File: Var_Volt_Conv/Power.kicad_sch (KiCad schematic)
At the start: 67 parts

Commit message: Annotated schematic symbols
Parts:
- gave numbers to parts that had none: 67

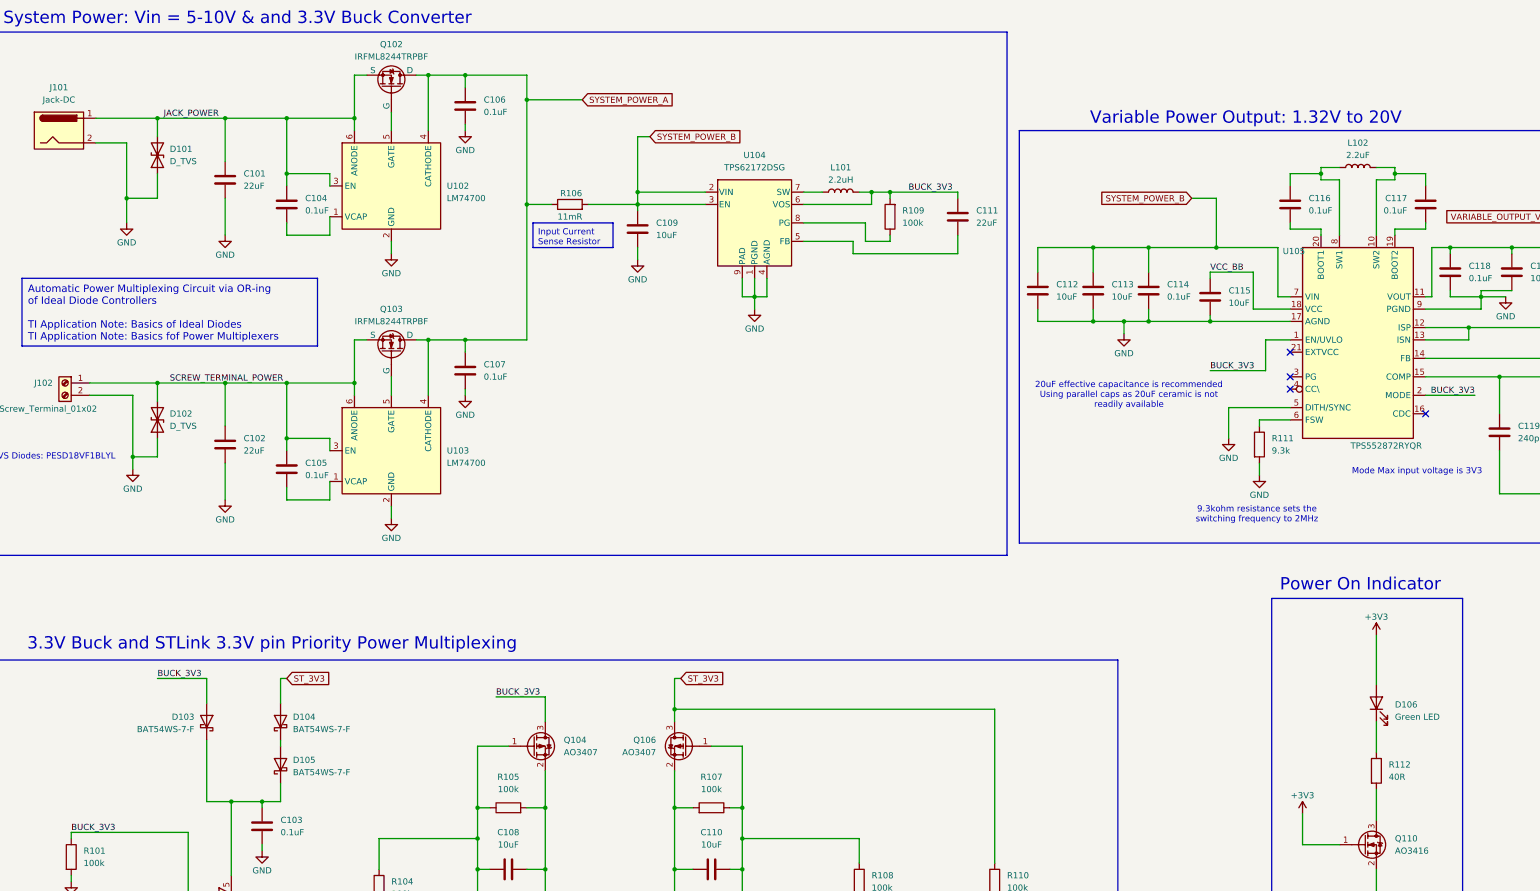
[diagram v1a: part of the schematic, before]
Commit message: Fixed ERC issues
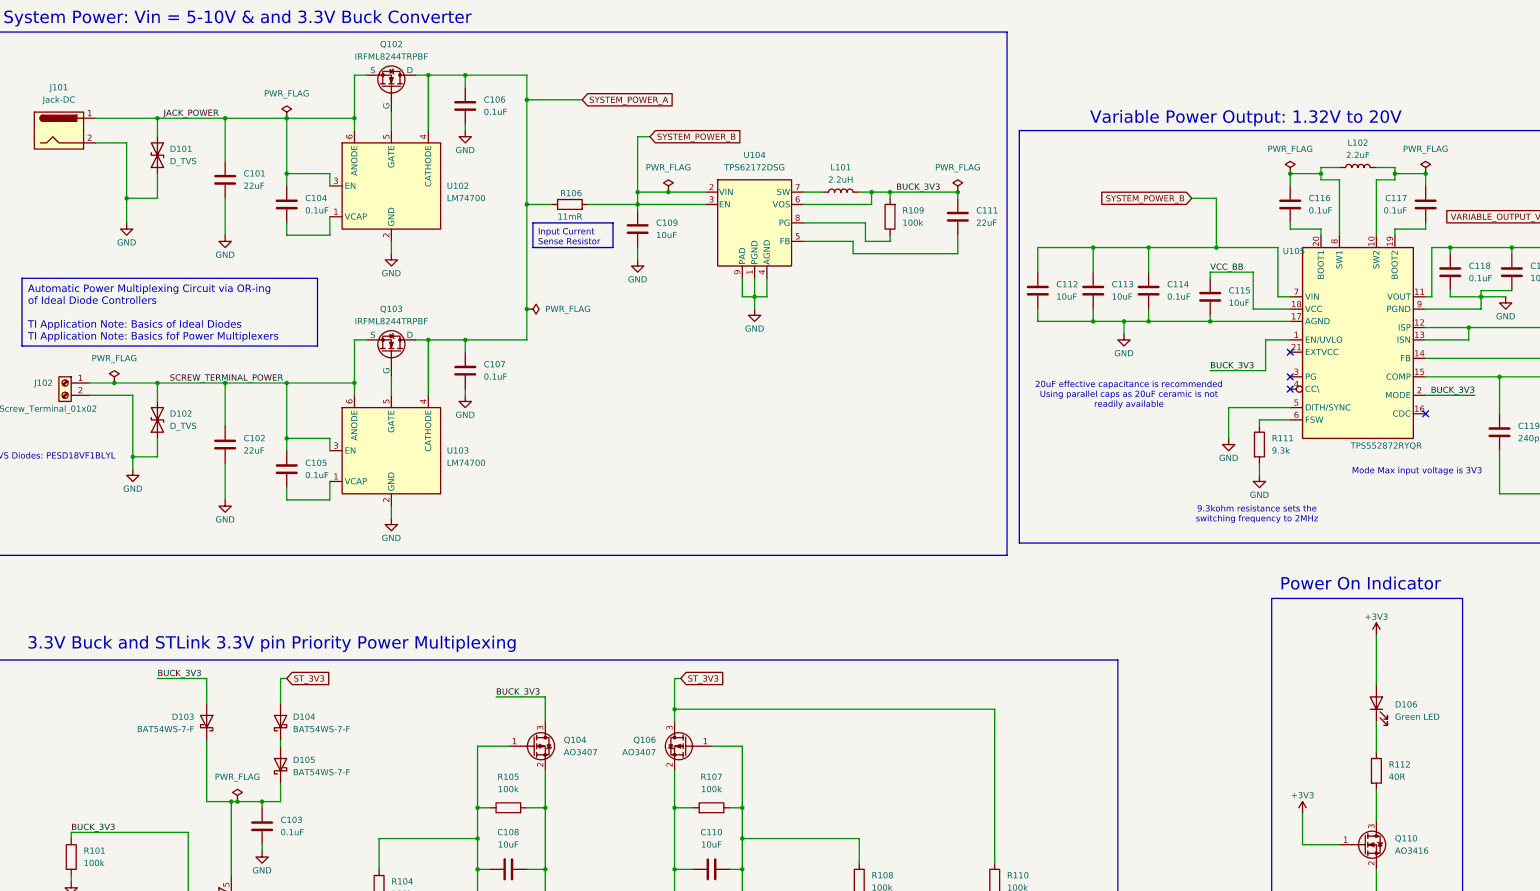
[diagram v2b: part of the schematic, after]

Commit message: Add footprints and correct LCD pin numbering
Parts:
- D102: footprint (none) -> Diode_SMD:D_SOD-882
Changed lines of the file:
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@@
 			)
 		)
-		(property "Footprint" ""
+		(property "Footprint" "Diode_SMD:D_SOD-882"
 			(at 52.07 135.89 0)
 			(effects

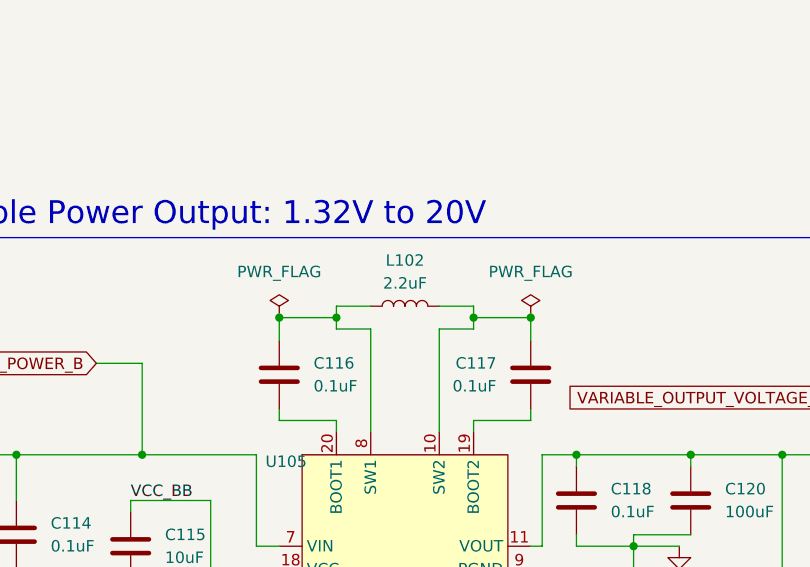
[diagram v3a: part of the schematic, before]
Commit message: Add footprints for all capacitors, and record cap part names
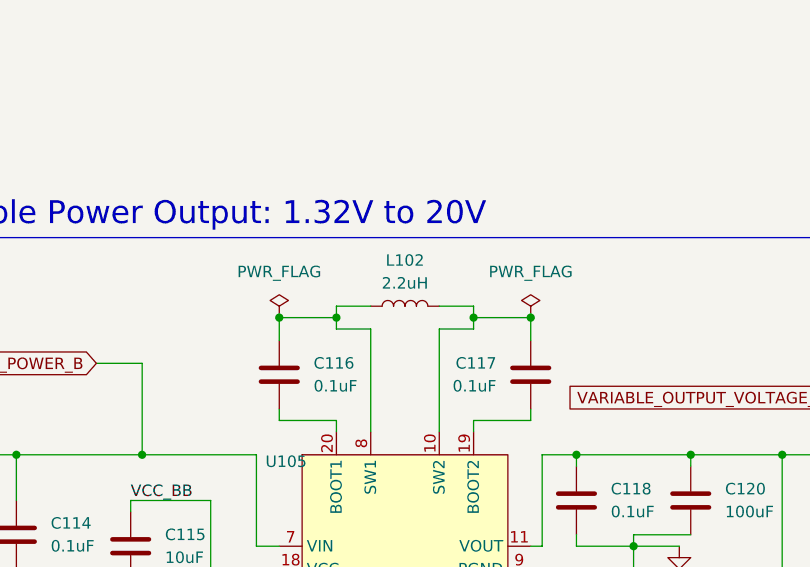
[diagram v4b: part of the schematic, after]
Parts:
- C101, C102, C111: footprint (none) -> Capacitor_SMD:C_1206_3216Metric
- C103, C104, C105, C106, C107, C114, C116, C117, C118, C121: footprint (none) -> Capacitor_SMD:C_0402_1005Metric
- C108, C109, C110, C112, C113, C115: footprint (none) -> Capacitor_SMD:C_0805_2012Metric
- C119, C122, C123: footprint (none) -> Capacitor_SMD:C_0603_1608Metric
- C120: footprint (none) -> Capacitor_SMD:CP_Elec_6.3x7.7
- L102: value 2.2uF -> 2.2uH
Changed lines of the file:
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@@
 			)
 		)
-		(property "Footprint" ""
+		(property "Footprint" "Capacitor_SMD:C_0402_1005Metric"
 			(at 79.7052 95.25 0)
 			(effects
@@
 			)
 		)
-		(property "Footprint" ""
+		(property "Footprint" "Capacitor_SMD:C_1206_3216Metric"
 			(at 67.0052 144.78 0)
 			(effects
@@
 			)
 		)
-		(property "Footprint" ""
+		(property "Footprint" "Capacitor_SMD:C_0402_1005Metric"
 			(at 257.5052 113.03 0)
 			(effects
@@
 			)
 		)
-		(property "Footprint" ""
+		(property "Footprint" "Capacitor_SMD:C_0402_1005Metric"
 			(at 74.6252 223.52 0)
 			(effects
@@
 			)
 		)
-		(property "Footprint" ""
+		(property "Footprint" "Capacitor_SMD:CP_Elec_6.3x7.7"
 			(at 332.4352 109.22 0)
 			(effects
@@
 			)
 		)
-		(property "Footprint" ""
+		(property "Footprint" "Capacitor_SMD:C_0402_1005Metric"
 			(at 345.1352 149.86 0)
 			(effects
@@
 			)
 		)
-		(property "Footprint" ""
+		(property "Footprint" "Capacitor_SMD:C_1206_3216Metric"
 			(at 218.1352 97.79 0)
 			(effects
@@
 			)
 		)
-		(property "Footprint" ""
+		(property "Footprint" "Capacitor_SMD:C_0805_2012Metric"
 			(at 128.27 227.6348 0)
 			(effects
@@
 			)
 		)
-		(property "Footprint" ""
+		(property "Footprint" "Capacitor_SMD:C_0805_2012Metric"
 			(at 234.6452 113.03 0)
 			(effects
@@
 			)
 		)
-		(property "Footprint" ""
+		(property "Footprint" "Capacitor_SMD:C_0603_1608Metric"
 			(at 354.0252 201.93 0)
 			(effects
@@
 			)
 		)
-		(property "Footprint" ""
+		(property "Footprint" "Capacitor_SMD:C_0603_1608Metric"
 			(at 388.3152 201.93 0)
 			(effects
@@
 			)
 		)
-		(property "Footprint" ""
+		(property "Footprint" "Capacitor_SMD:C_0402_1005Metric"
 			(at 79.7052 149.86 0)
 			(effects
@@
 			)
 		)
-		(property "Footprint" ""
+		(property "Footprint" "Capacitor_SMD:C_0805_2012Metric"
 			(at 246.0752 113.03 0)
 			(effects
@@
 			)
 		)
-		(property "Value" "2.2uF"
+		(property "Value" "2.2uH"
 			(at 299.72 81.28 90)
 			(effects
@@
 			)
 		)
-		(property "Footprint" ""
+		(property "Footprint" "Capacitor_SMD:C_0603_1608Metric"
 			(at 329.8952 142.24 0)
 			(effects
@@
 			)
 		)
-		(property "Footprint" ""
+		(property "Footprint" "Capacitor_SMD:C_0402_1005Metric"
 			(at 116.5352 129.54 0)
 			(effects
@@
 			)
 		)
-		(property "Footprint" ""
+		(property "Footprint" "Capacitor_SMD:C_0402_1005Metric"
 			(at 312.7248 95.25 0)
 			(effects
@@
 			)
 		)
-		(property "Footprint" ""
+		(property "Footprint" "Capacitor_SMD:C_0805_2012Metric"
 			(at 270.2052 114.3 0)
 			(effects
@@
 			)
 		)
-		(property "Footprint" ""
+		(property "Footprint" "Capacitor_SMD:C_0402_1005Metric"
 			(at 286.7152 95.25 0)
 			(effects
@@
 			)
 		)
-		(property "Footprint" ""
+		(property "Footprint" "Capacitor_SMD:C_0402_1005Metric"
 			(at 116.5352 74.93 0)
 			(effects
@@
 			)
 		)
-		(property "Footprint" ""
+		(property "Footprint" "Capacitor_SMD:C_1206_3216Metric"
 			(at 67.0052 90.17 0)
 			(effects
@@
 			)
 		)
-		(property "Footprint" ""
+		(property "Footprint" "Capacitor_SMD:C_0805_2012Metric"
 			(at 152.0952 100.33 0)
 			(effects
@@
 			)
 		)
-		(property "Footprint" ""
+		(property "Footprint" "Capacitor_SMD:C_0402_1005Metric"
 			(at 319.7352 109.22 0)
 			(effects
@@
 			)
 		)
-		(property "Footprint" ""
+		(property "Footprint" "Capacitor_SMD:C_0805_2012Metric"
 			(at 162.56 227.6348 0)
 			(effects

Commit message: Add inductor footprint
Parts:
- L101, L102: footprint (none) -> Inductor_SMD:L_Sunlord_MWSA0503S
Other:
- note added: "System Power: Vin = 3-17V & and 3.3V Buck Converter"
- note removed: "System Power: Vin = 5-10V & and 3.3V Buck Converter"
- moved on the sheet: C101, C102, C103, C104, C105, C106, C107, C108, C109, C110, C111, C112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

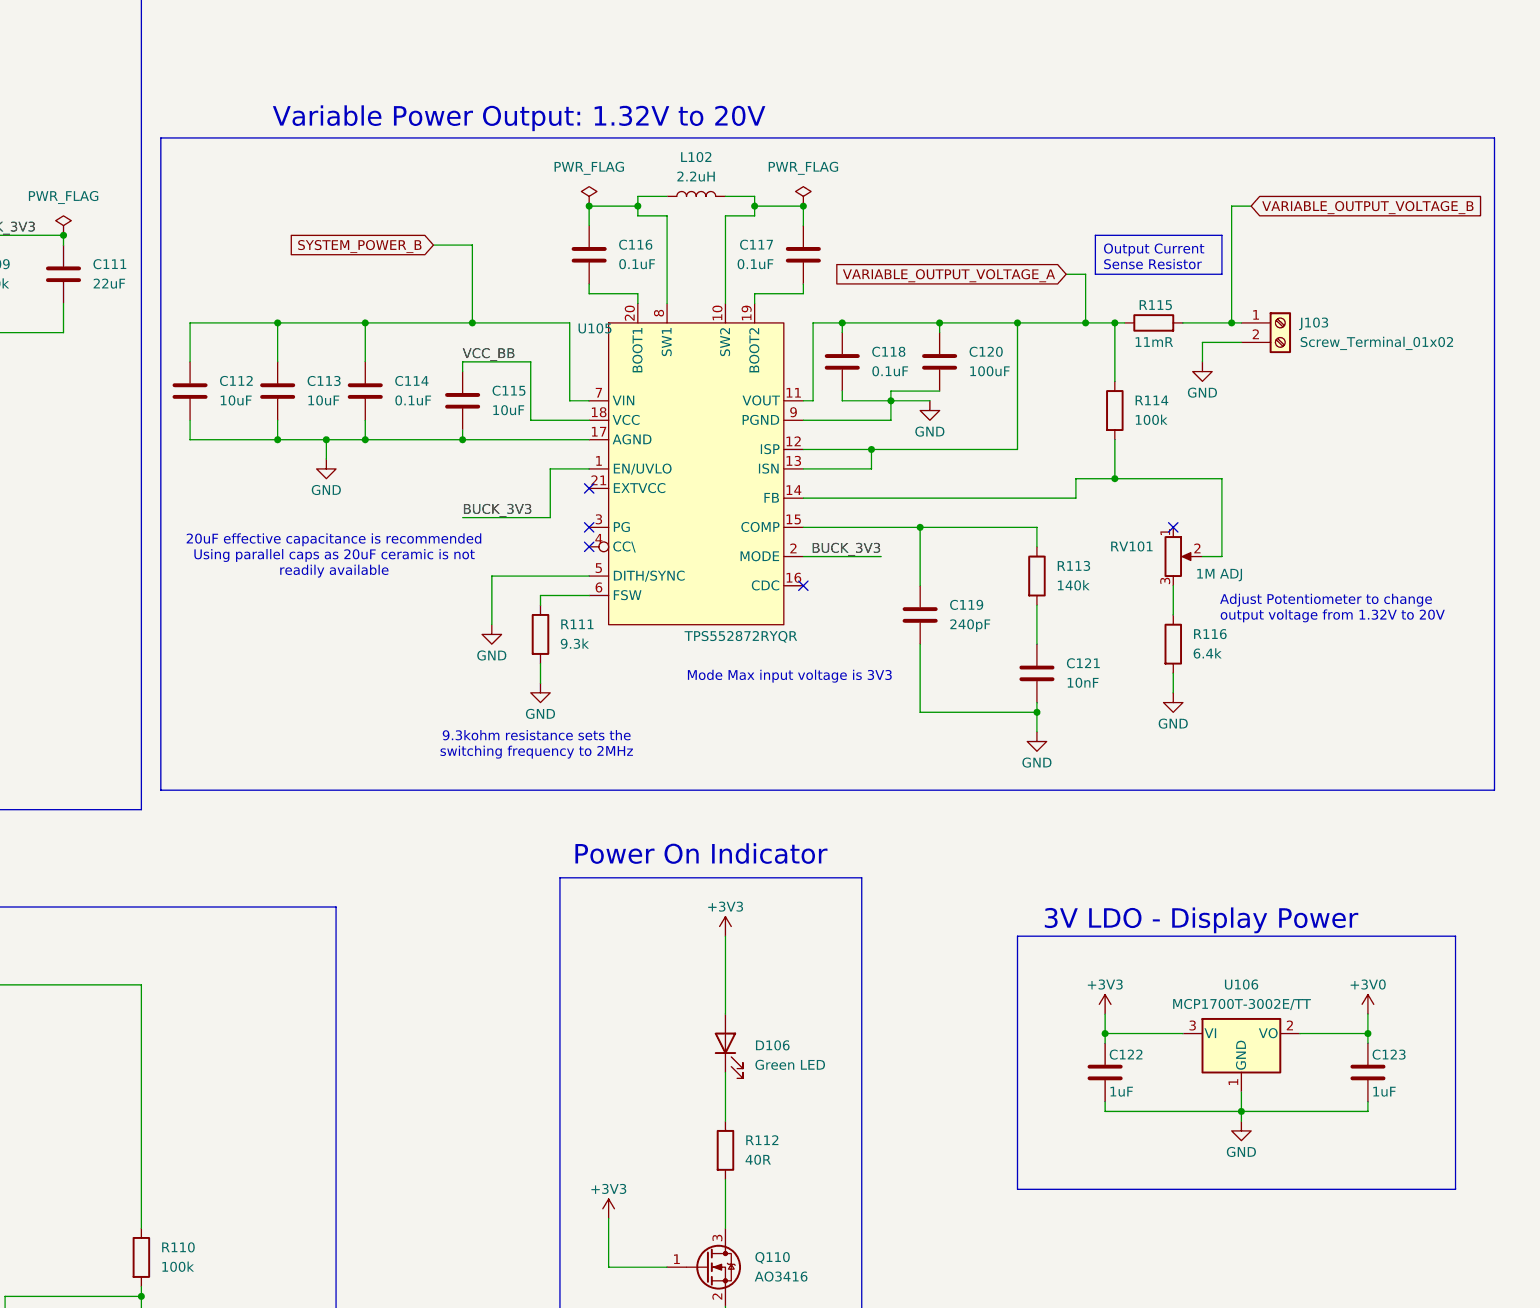
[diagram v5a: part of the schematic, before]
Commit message: Added footprints to all components except the connectors and buck-boost converter
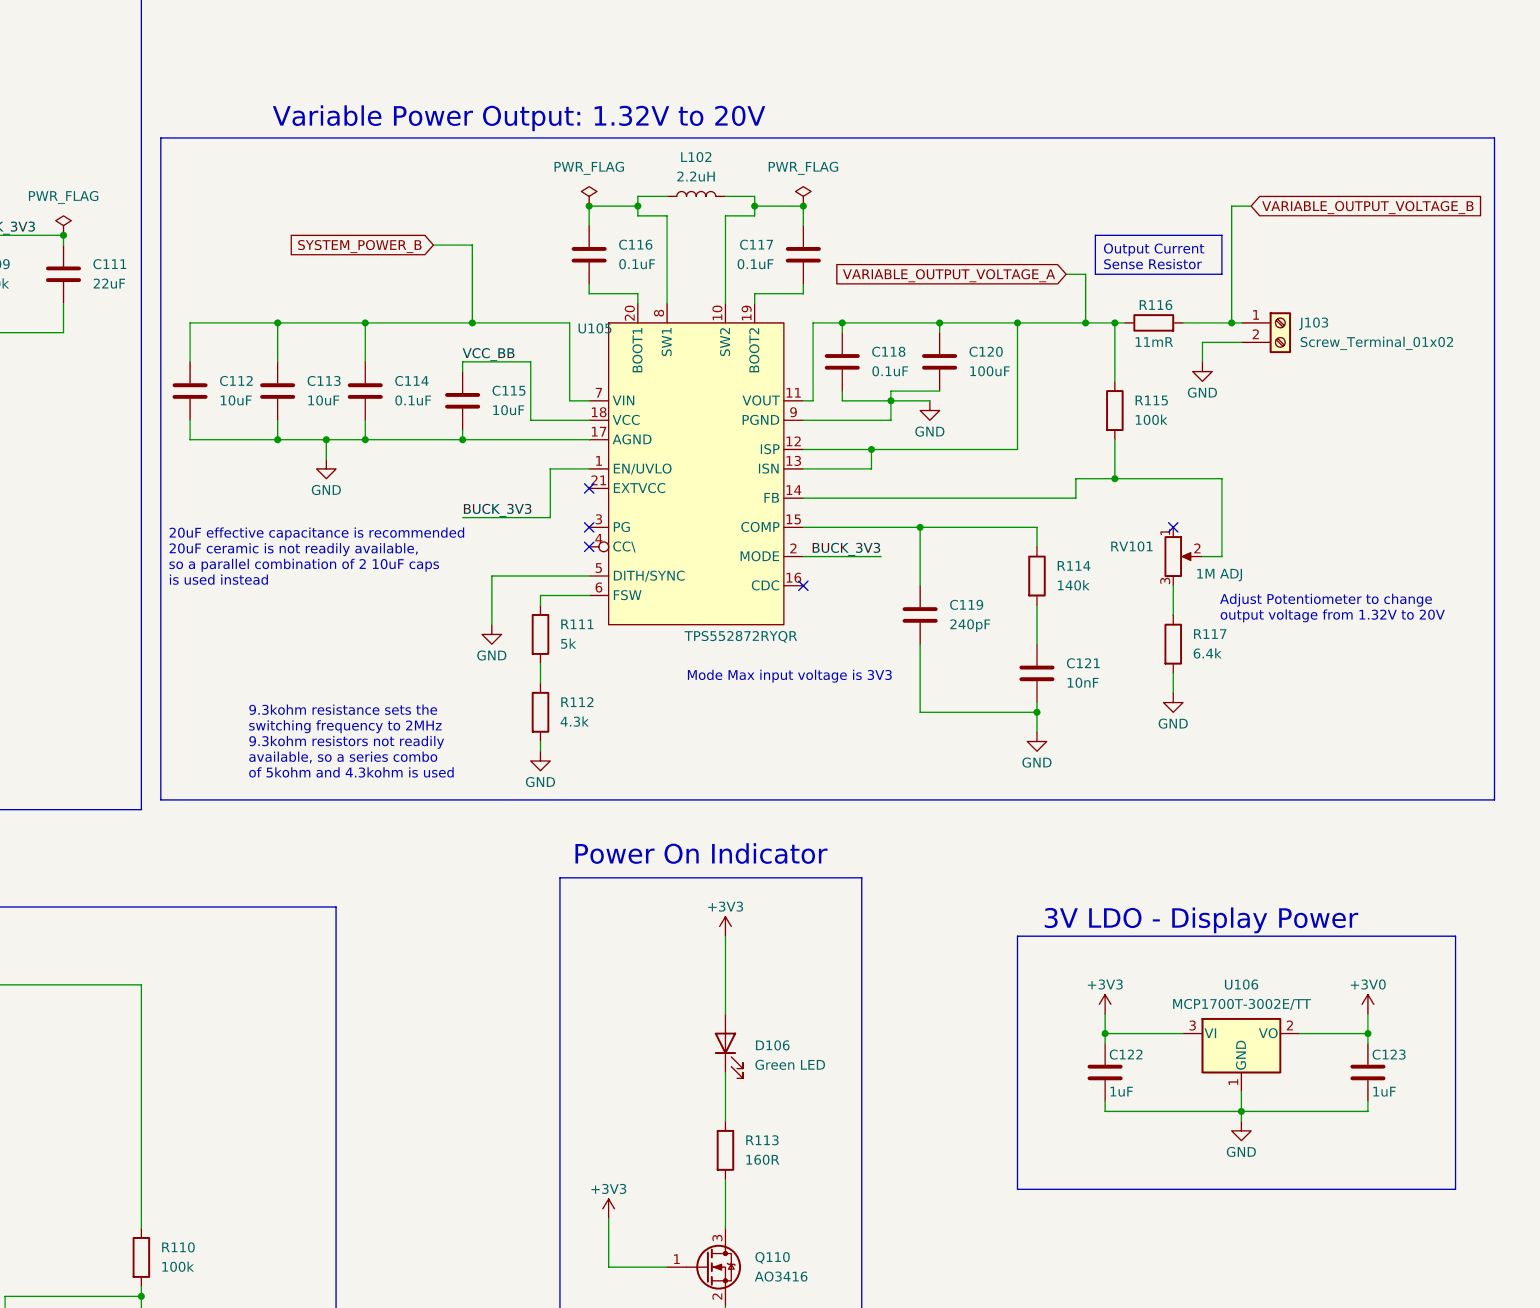
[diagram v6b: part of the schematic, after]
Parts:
- added R112: 4.3k, Resistor_SMD:R_0805_2012Metric, symbol Device:R
- R101, R102, R103, R104, R105, R107, R108, R109, R110: footprint (none) -> Resistor_SMD:R_0402_1005Metric
- R106: footprint (none) -> Resistor_SMD:R_1210_3225Metric
- R111: value 9.3k -> 5k; footprint (none) -> Resistor_SMD:R_0603_1608Metric
- R113: renamed from R112; value 40R -> 160R; footprint (none) -> Resistor_SMD:R_0603_1608Metric
- R114: renamed from R113; footprint (none) -> Resistor_SMD:R_0603_1608Metric
- R115: renamed from R114; footprint (none) -> Resistor_SMD:R_0402_1005Metric
- R116: renamed from R115; footprint (none) -> Resistor_SMD:R_1210_3225Metric
- R117: renamed from R116; footprint (none) -> Resistor_SMD:R_0603_1608Metric
- RV101: footprint (none) -> Potentiometer_THT:Potentiometer_Bourns_PTV09A-1_Single_Vertical
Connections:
- net GND: now also R112.2; no longer R111.2
- new net: R111.2, R112.1
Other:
- note added: "20uF effective capacitance is recommended 20uF ceramic is not readily available, so a parallel combination of 2 10uF caps is used instead"
- note added: "9.3kohm resistance sets the switching frequency to 2MHz 9.3kohm resistors not readily available, so a series combo of 5kohm and 4.3kohm is used"
- note removed: "20uF effective capacitance is recommended Using parallel caps as 20uF ceramic is not readily available"
- note removed: "9.3kohm resistance sets the switching frequency to 2MHz"

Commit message: Assign footprints to all footprints except the buck-boost converter
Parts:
- J101: footprint (none) -> Connector_BarrelJack:BarrelJack_CUI_PJ-063AH_Horizontal
- J102, J103: footprint (none) -> TerminalBlock_4Ucon:TerminalBlock_4Ucon_1x02_P3.50mm_Vertical
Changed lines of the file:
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@@
 			)
 		)
-		(property "Footprint" ""
+		(property "Footprint" "TerminalBlock_4Ucon:TerminalBlock_4Ucon_1x02_P3.50mm_Vertical"
 			(at 34.29 109.22 0)
 			(effects
@@
 			)
 		)
-		(property "Footprint" ""
+		(property "Footprint" "Connector_BarrelJack:BarrelJack_CUI_PJ-063AH_Horizontal"
 			(at 34.29 58.166 0)
 			(effects
@@
 			)
 		)
-		(property "Footprint" ""
+		(property "Footprint" "TerminalBlock_4Ucon:TerminalBlock_4Ucon_1x02_P3.50mm_Vertical"
 			(at 377.19 81.28 0)
 			(effects

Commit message: Created and added footprint for buck-boost converter
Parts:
- U105: footprint (none) -> Buck_Boost:21-PowerVFQFN
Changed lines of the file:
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@@
 			)
 		)
-		(property "Footprint" ""
+		(property "Footprint" "Buck_Boost:21-PowerVFQFN"
 			(at 349.25 59.69 0)
 			(effects
